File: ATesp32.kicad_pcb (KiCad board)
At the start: 2 copper layers, 61 parts, among them J1 USB_C_Receptacle_USB2.0_16P, J2 JST PH, Q1 DMP2045U, SW1 SW_Push, SW2 SW_Push, U1 ESP32-S3, U2 ATmega32A-P, U3 MCP73831-2-OT, U4 AP2112K-3.3, U5 CP2102N-Axx-xQFN24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

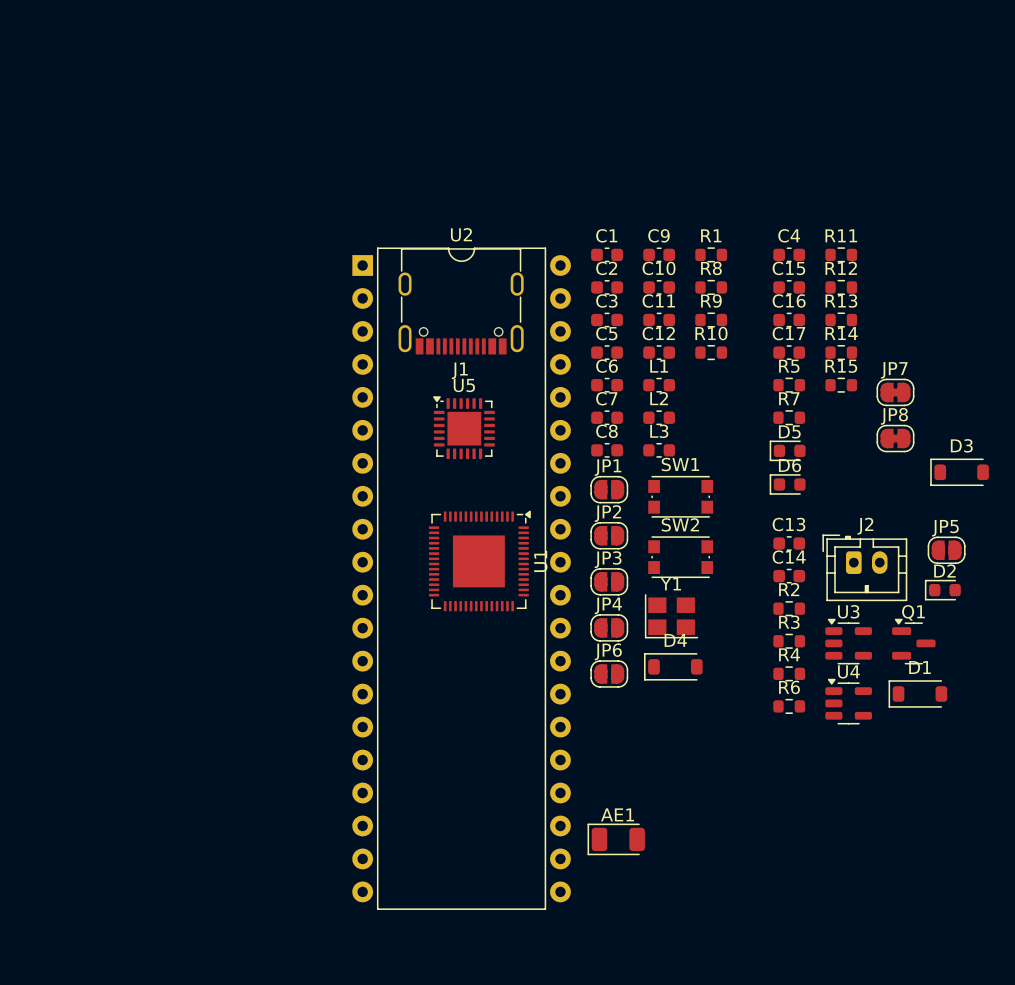
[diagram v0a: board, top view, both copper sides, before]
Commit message: remove misc superfluous components
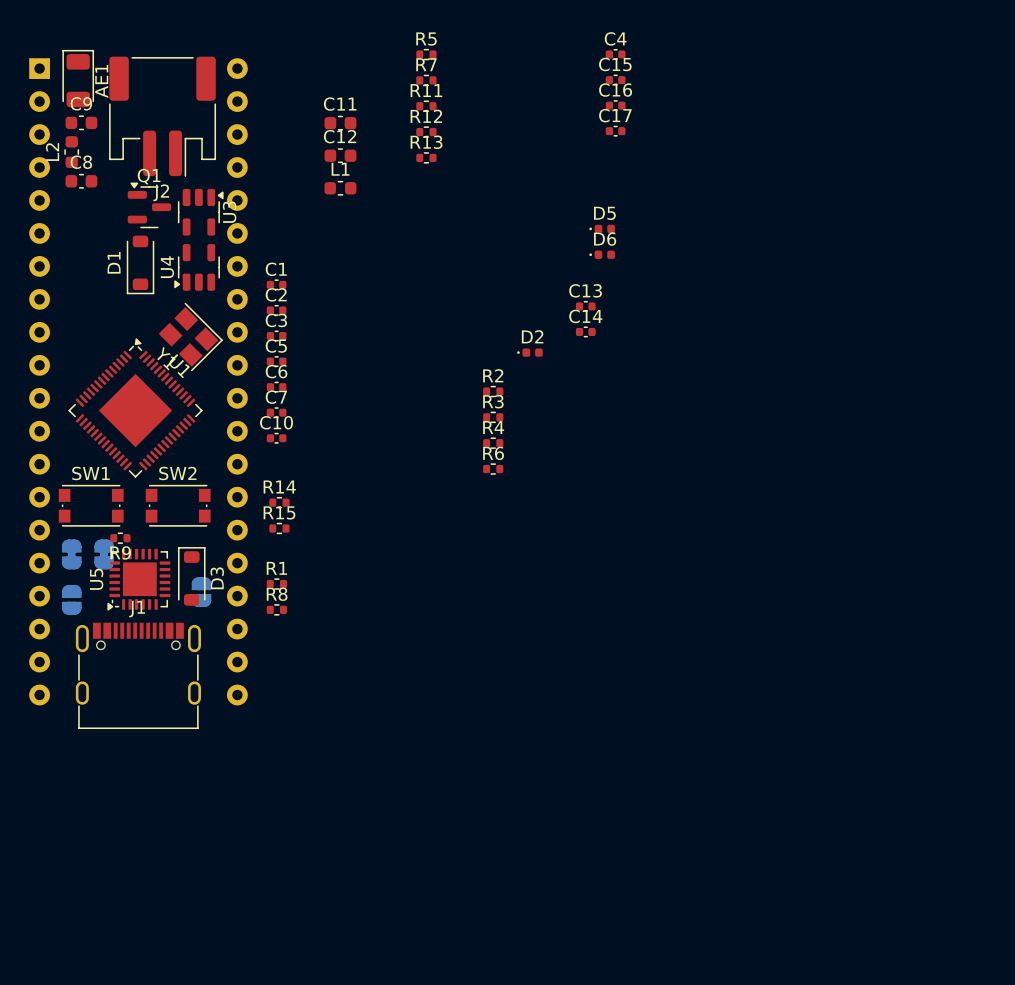
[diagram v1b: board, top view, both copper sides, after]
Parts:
- removed D4: MBR0540, Diode_SMD:D_SOD-123
- removed JP1, JP2, JP3, JP5: SolderJumper_2_Open, Jumper:SolderJumper-2_P1.3mm_Open_RoundedPad1.0x1.5mm
- removed L3: 24nH, Inductor_SMD:L_0603_1608Metric
- removed R10: 10K, Resistor_SMD:R_0603_1608Metric
- C1, C10, C13, C14, C15, C16, C17, C2, C3, C4, C5, C6, C7: footprint Capacitor_SMD:C_0603_1608Metric -> Capacitor_SMD:C_0402_1005Metric
- D2, D5, D6: footprint LED_SMD:LED_0603_1608Metric -> LED_SMD:LED_0402_1005Metric
- J2: footprint Connector_JST:JST_PH_B2B-PH-K_1x02_P2.00mm_Vertical -> Connector_JST:JST_PH_S2B-PH-SM4-TB_1x02-1MP_P2.00mm_Horizontal
- JP4, JP6, JP7, JP8: moved to B.Cu
- R1, R11, R12, R13, R14, R15, R2, R3, R4, R5, R6, R7, R8, R9: footprint Resistor_SMD:R_0603_1608Metric -> Resistor_SMD:R_0402_1005Metric
- moved AE1 71.8 mm to (47.0, 34.8), turned to -90 degrees
- moved D1 68.6 mm to (51.8, 48.8), turned to 90 degrees
- moved Q1 67.8 mm to (52.5, 44.5)
- moved JP7 64.7 mm to (46.5, 71.2), turned to 90 degrees
- moved J2 63.4 mm to (53.5, 37.5), turned to 180 degrees
- moved JP8 61.6 mm to (49.0, 71.2), turned to 90 degrees
- moved U4 60.3 mm to (56.3, 49.1), turned to 90 degrees
- moved U3 60.1 mm to (56.3, 44.9), turned to -90 degrees
- moved D3 59.9 mm to (55.8, 73.1), turned to -90 degrees
- moved L2 49.7 mm to (46.5, 40.2), turned to 90 degrees
- moved R9 48.5 mm to (50.2, 70.0), turned to 180 degrees
- moved C9 45.7 mm to (47.2, 38.0)
- moved C8 45.5 mm to (47.2, 42.5)
- moved SW1 45.4 mm to (48.0, 67.5)
- moved R14 44.8 mm to (62.5, 67.3)
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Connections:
- C11 pad 2: Net-(JP1-A) -> Net-(U1-XTAL_P)
- R6 pad 1: Net-(JP5-A) -> Net-(U3-STAT)
- U1 pad 10: PA4 -> PB4
- U1 pad 11: PA5 -> PB5
- U1 pad 12: PA6 -> PA0
- U1 pad 13: PA7 -> PA1
- U1 pad 14: PB0 -> PA2
- U1 pad 15: PB1 -> PA3
- U1 pad 16: PB2 -> PA4
- U1 pad 17: PB3 -> PA5
- U1 pad 18: PB4 -> PA6
- U1 pad 19: PB5 -> PA7
- U1 pad 25: PD2 -> PD3_N
- U1 pad 26: PD3 -> PD2_P
- U1 pad 6: PA0 -> PB0
- U1 pad 7: PA1 -> PB1
- U1 pad 8: PA2 -> PB2
- U1 pad 9: PA3 -> PB3
- U2 pad 10: Net-(D4-A) -> +5V
- U2 pad 12: XTAL2 -> unconnected-(U2-XTAL2-Pad12)
- U2 pad 13: XTAL1 -> unconnected-(U2-XTAL1-Pad13)
- U2 pad 16: PD2 -> PD2_P
- U2 pad 17: PD3 -> PD3_N
- U2 pad 30: Net-(D4-A) -> +5V
- U2 pad 9: RESET -> unconnected-(U2-~{RESET}-Pad9)
- U3 pad 1: Net-(JP5-B) -> Net-(U3-STAT)
- Y1 pad 3: Net-(JP1-A) -> Net-(U1-XTAL_P)

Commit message: first pass at component placement
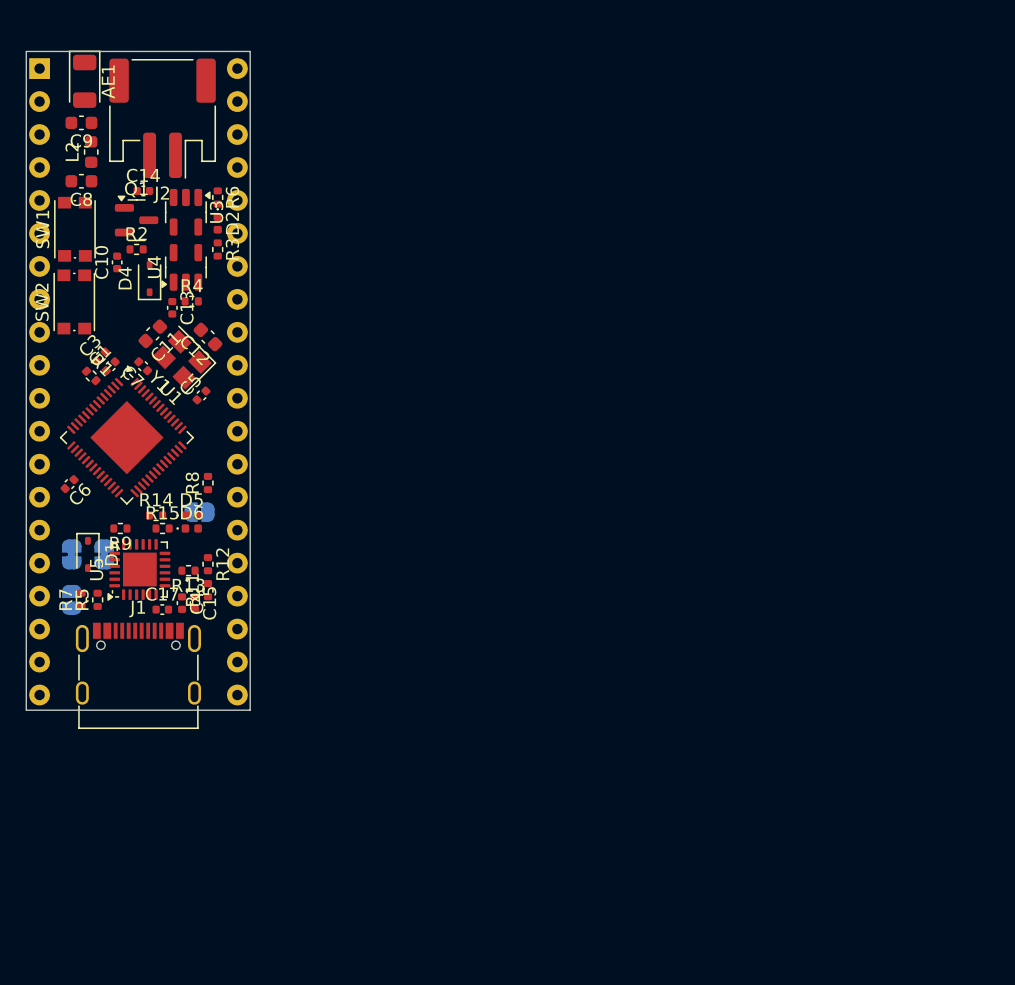
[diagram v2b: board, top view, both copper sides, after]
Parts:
- removed C16, C2: 0.1uF, Capacitor_SMD:C_0402_1005Metric
- removed D3: MBR0540, Diode_SMD:D_SOD-123
- removed L1: 2.7nH, Inductor_SMD:L_0603_1608Metric
- added D4: NSR0320, Diode_SMD:D_SOD-323, F.Cu at (52.5, 50.0)
- D1: value MBR0540 -> NSR0320; footprint Diode_SMD:D_SOD-123 -> Diode_SMD:D_SOD-323
- moved C4 53.9 mm to (55.0, 75.0), turned to -90 degrees
- moved C15 51.7 mm to (56.0, 75.0), turned to -90 degrees
- moved C17 50.8 mm to (53.5, 75.5)
- moved R5 49.1 mm to (48.5, 74.8), turned to 90 degrees
- moved R7 48.0 mm to (47.2, 74.8), turned to 90 degrees
- moved R11 40.9 mm to (57.0, 74.0), turned to 90 degrees
- moved D5 38.7 mm to (55.8, 68.2)
- moved D6 38.2 mm to (55.8, 69.2)
- moved R12 37.3 mm to (57.0, 72.0), turned to -90 degrees
- moved R13 36.7 mm to (55.5, 72.5), turned to 180 degrees
- moved C14 35.8 mm to (52.0, 43.2)
- moved C13 31.9 mm to (54.2, 52.2), turned to -90 degrees
- moved R6 29.8 mm to (57.8, 43.8), turned to -90 degrees
- moved R2 29.6 mm to (51.5, 47.8)
- moved D2 26.2 mm to (57.8, 45.8), turned to -90 degrees
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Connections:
- C1 pad 1: Net-(C1-Pad1) -> +3V3
- C13 pad 1: Net-(D1-K) -> Net-(D4-K)
- D1 pad 1: Net-(D1-K) -> +5V
- D1 pad 2: +5V -> Net-(D1-A)
- J1 pad A4: Net-(D3-A) -> Net-(D1-A)
- J1 pad A9: Net-(D3-A) -> Net-(D1-A)
- J1 pad B4: Net-(D3-A) -> Net-(D1-A)
- J1 pad B9: Net-(D3-A) -> Net-(D1-A)
- Q1 pad 3: Net-(D1-K) -> Net-(D4-K)
- R4 pad 1: Net-(D1-K) -> Net-(D4-K)
- U1 pad 2: Net-(C1-Pad1) -> +3V3
- U1 pad 3: Net-(C1-Pad1) -> +3V3
- U4 pad 1: Net-(D1-K) -> Net-(D4-K)
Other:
- board outline added: 17.2 x 50.8 mm

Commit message: centered headers and USB-C. Set grid and drill origins
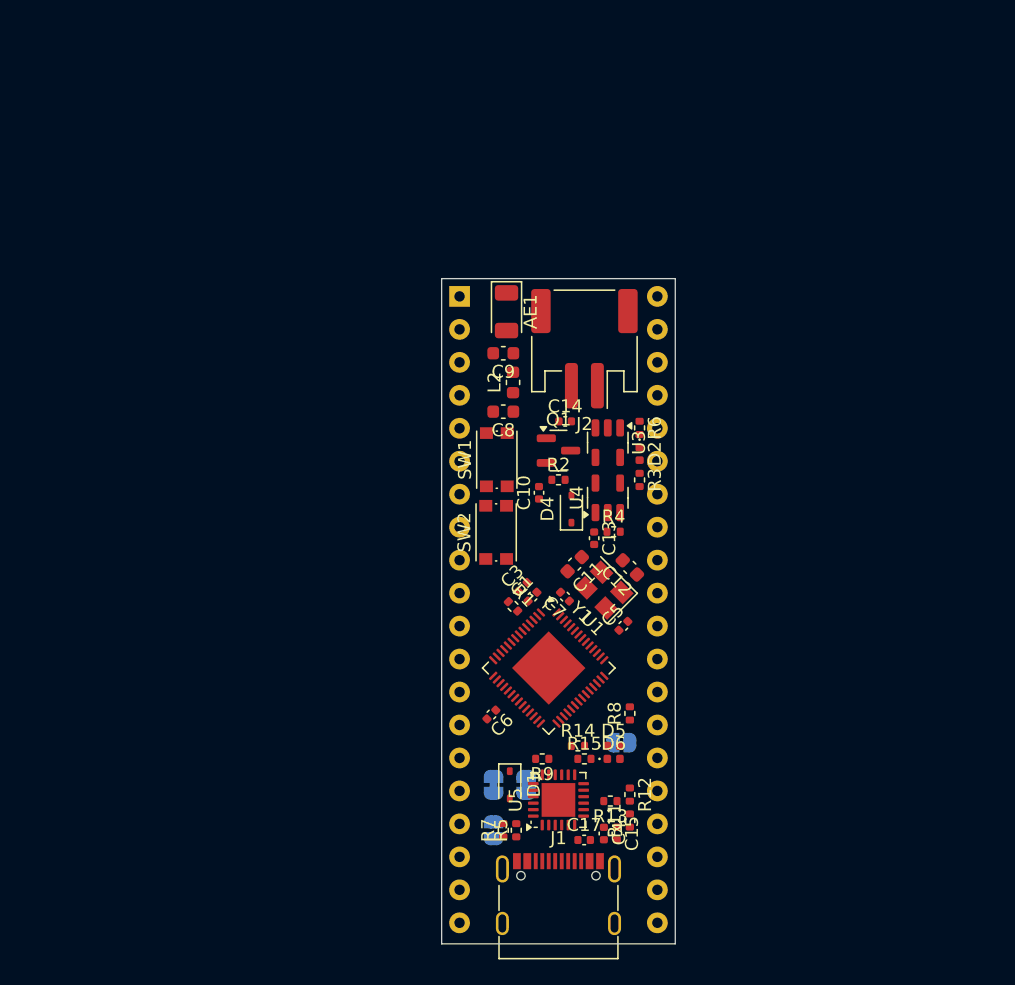
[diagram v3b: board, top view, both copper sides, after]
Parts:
- moved C17 37.0 mm to (86.0, 93.2)
- moved C6 37.0 mm to (78.8, 83.6)
- moved AE1 37.0 mm to (80.0, 52.5)
- moved C1 37.0 mm to (82.0, 74.5)
- moved C10 37.0 mm to (82.5, 66.5)
- moved C11 37.0 mm to (85.2, 72.0)
- moved C12 37.0 mm to (89.5, 72.2)
- moved C13 37.0 mm to (86.8, 70.0)
- moved C15 37.0 mm to (88.5, 92.8)
- moved C3 37.0 mm to (81.2, 73.8)
- moved C4 37.0 mm to (87.5, 92.8)
- moved C5 37.0 mm to (89.0, 76.8)
- moved C7 37.0 mm to (84.5, 74.5)
- moved C8 37.0 mm to (79.8, 60.2)
- moved C9 37.0 mm to (79.8, 55.8)
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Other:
- board size 17.2 x 50.8 mm -> 18 x 51.2 mm

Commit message: Finished layout, need to fix silk
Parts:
- moved R1 9.48 mm to (79.8, 65.8), turned to 0 degrees
- moved R8 3.13 mm to (86.8, 85.0), turned to 180 degrees
- moved D1 3.00 mm to (80.3, 92.0)
- moved C10 2.77 mm to (79.8, 66.8), turned to 180 degrees
- moved C1 1.71 mm to (80.4, 75.1), turned to -135 degrees
- moved C3 1.68 mm to (79.7, 74.4), turned to -135 degrees
- moved R5 1.68 mm to (82.2, 93.2), turned to 180 degrees
- moved SW1 1.46 mm to (79.4, 62.5)
- moved C8 1.45 mm to (79.8, 58.8)
- moved R11 1.38 mm to (88.5, 90.8)
- moved R12 1.38 mm to (88.5, 88.8)
- moved C5 1.25 mm to (88.0, 77.5)
- moved JP8 1.20 mm to (81.5, 87.8)
- moved JP6 1.11 mm to (88.5, 86.8), turned to 180 degrees
- moved R2 1.00 mm to (85.0, 65.5)
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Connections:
- net Net-(U1-XTAL_N) renamed XTAL_N
- net Net-(U1-XTAL_P) renamed XTAL_P
- net PD2_P renamed D_P
- net PD3_N renamed D_N
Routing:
- net PA0: track 0.00 -> 33.7 mm, vias 0 -> 1
- net PA1: track 0.00 -> 31.5 mm, vias 0 -> 1
- net PD6: track 0.00 -> 30.7 mm, vias 0 -> 1
- net PA2: track 0.00 -> 29.2 mm, vias 0 -> 1
- net PB0: track 0.00 -> 27.8 mm, vias 0 -> 1
- net PA3: track 0.00 -> 26.9 mm, vias 0 -> 1
- net Net-(JP4-B): track 0.00 -> 26.7 mm, vias 0 -> 3
- net PD7: track 0.00 -> 25.9 mm, vias 0 -> 1
- net PB1: track 0.00 -> 25.5 mm, vias 0 -> 1
- net GND: track 0.00 -> 25.4 mm, vias 0 -> 39
- net PA4: track 0.00 -> 24.6 mm, vias 0 -> 1
- net PB2: track 0.00 -> 23.3 mm, vias 0 -> 1
- net PA5: track 0.00 -> 22.2 mm, vias 0 -> 1
- net PB3: track 0.00 -> 20.7 mm, vias 0 -> 1
- net PA6: track 0.00 -> 19.9 mm, vias 0 -> 1
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- added copper zone on F.Cu, net +3V3
- added copper zone on In2.Cu, net +3V3
- added copper zone on F.Cu, net +5V
- added copper zone on In2.Cu, net +5V
- added copper zone on F.Cu, net +BATT
- added copper zone on F.Cu, net GND
- added copper zone on In1.Cu, net GND
- added copper zone on F.Cu, net Net-(D1-A)
- added copper zone on B.Cu, net Net-(D4-K)
- added copper zone on F.Cu, net Net-(D4-K)
- added copper zone on B.Cu, net Net-(U5-VDD)
- added copper zone on F.Cu, net Net-(U5-VDD)
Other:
- copper layers 2 -> 4

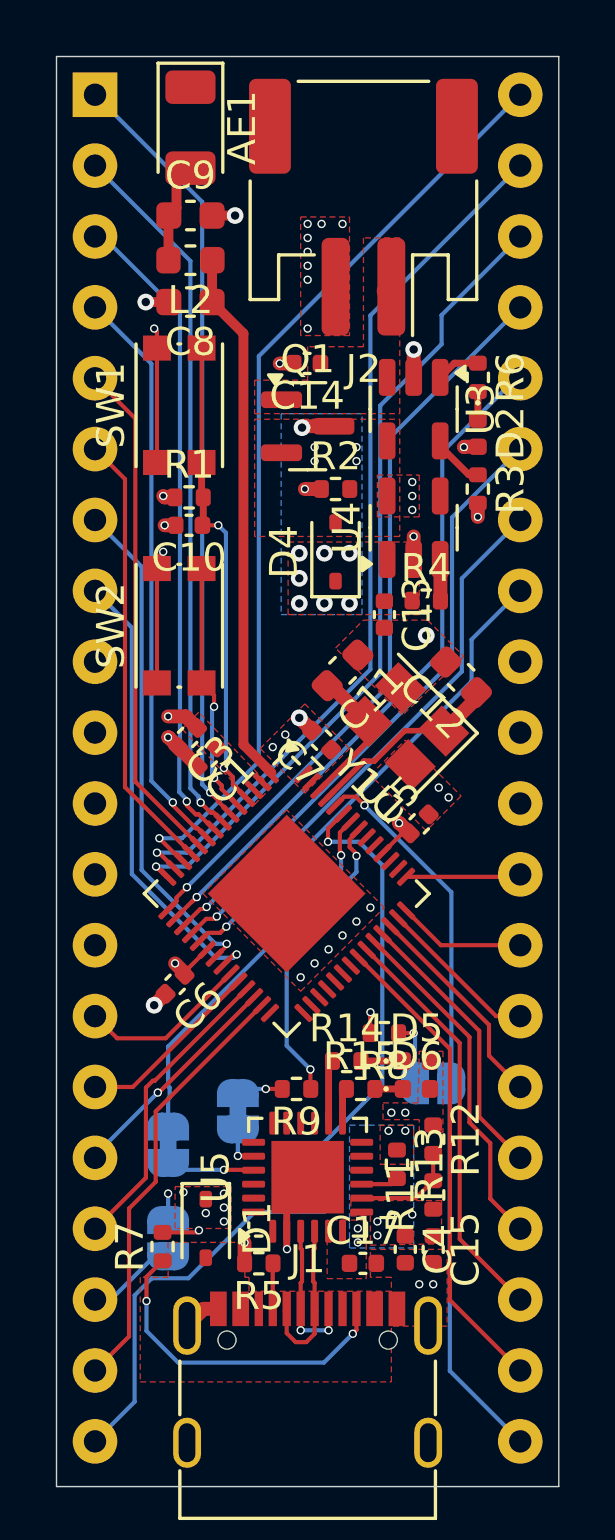
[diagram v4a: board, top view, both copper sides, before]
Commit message: fix USB routing
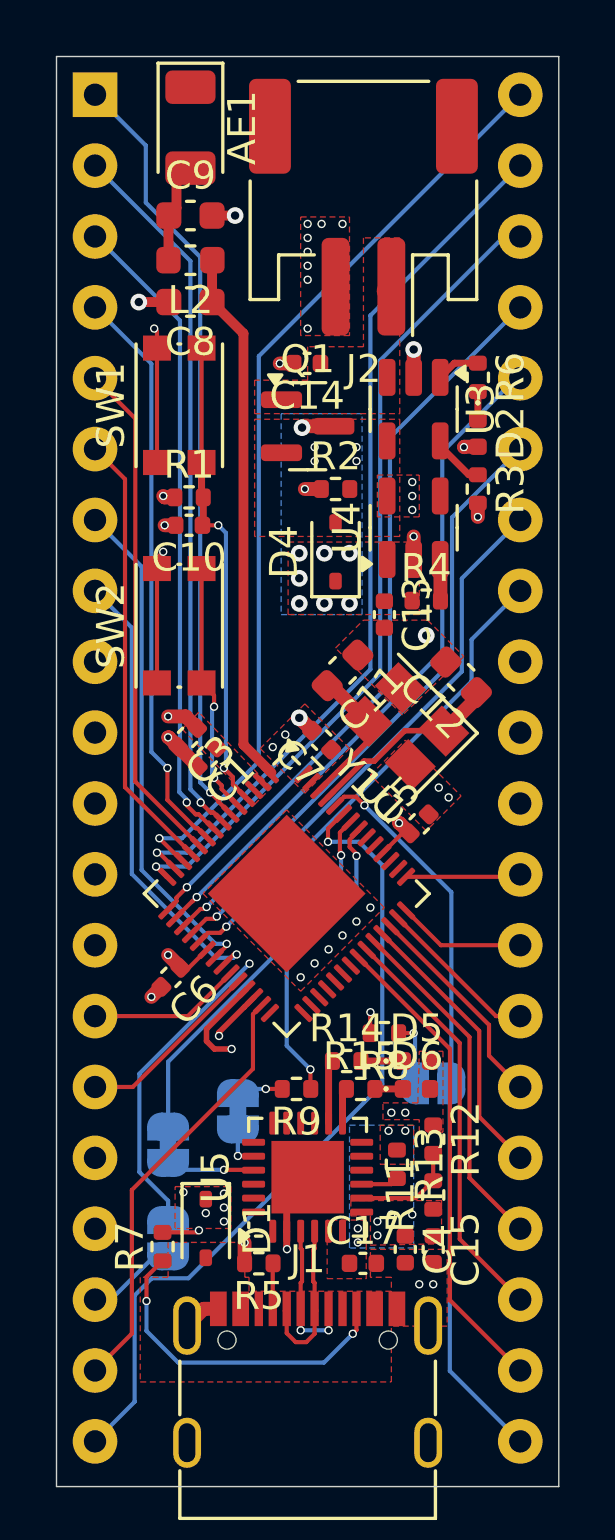
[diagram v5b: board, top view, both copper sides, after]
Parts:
- moved C6 0.29 mm to (79.1, 83.0)
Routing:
- net D_P: track 8.14 -> 11.9 mm
- net PD6: track 30.7 -> 29.2 mm
- net D_N: track 10.9 -> 11.9 mm, vias 0 -> 1
- net Net-(JP4-B): track 26.7 -> 27.5 mm
- net PD0: track 6.15 -> 5.49 mm
